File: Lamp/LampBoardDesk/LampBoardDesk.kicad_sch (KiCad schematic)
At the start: 87 parts, among them IC1 L7805ABD2T-TR, IC2 SN74LVC2T45DCUR, J1 DS1023-1x3SF11, J2 DS1023-1x3SF11, J3 284514-3, J4 DC-005-A250, Q1 CMN3406M, SW1 PEC11R, SW2 MT-0-102, U1 RP2040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

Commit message: boards are done
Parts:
- removed H4: MountingHole_Pad, MountingHole:MountingHole_2.7mm_M2.5_DIN965_Pad, symbol Mechanical:MountingHole_Pad
- removed J3: 284514-3, 284514-3:SHDR3W80P0X350_1X3_1250X725X940P, symbol 284514-3:284514-3
- added J3: 284514-3, easyeda2kicad:CONN-TH_3P-P3.50_15EDGRC-3.5-03P, symbol easyeda2kicad:15EDGRC-3.5-03P-14-00A(H)
- J1, J2: footprint easyeda2kicad:HDR-TH_3P-P2.54-V-F-1 -> easyeda2kicad:CONN-SMD-3P-P1.00_BM03B-SRSS-TB-LF-SN; symbol easyeda2kicad:DS1023-1X3SF11 -> easyeda2kicad:BM03B-SRSS-TB(LF)(SN); LCSC C7509516 -> C160389; LCSC Part C7509516 -> C160389
- SW2: footprint easyeda2kicad:SW-TH_MT-0-102-E001-T000-RS-PJ -> easyeda2kicad:SW-TH_MT-0-102-C004-N004-RS; symbol easyeda2kicad:MT-0-102-E001-T000-RS -> easyeda2kicad:MT-0-102-C004-N004-RS; LCSC C1788499 -> C1788496; LCSC Part C1788499 -> C1788496
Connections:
- net +24V: now also SW2.1, J3.3; no longer SW2.3
- net BOOT_LED: now also U1.30 (GPIO19); no longer U1.36 (GPIO24)
- net BTN: now also U1.38 (GPIO26_ADC0); no longer U1.8 (GPIO6)
- net BTN_LED: now also U1.39 (GPIO27_ADC1); no longer U1.7 (GPIO5)
- net ENC_A: now also U1.36 (GPIO24); no longer U1.14 (GPIO11)
- net ENC_B: now also U1.37 (GPIO25); no longer U1.13 (GPIO10)
- net GND: now also J1.4, J1.5, J2.4, J2.5, SW2.4, SW2.5
- net LED_D_O: now also J3.2
- net LED_EN: now also U1.29 (GPIO18); no longer U1.15 (GPIO12)
- net LED_EN_LED: now also U1.14 (GPIO11); no longer U1.4 (GPIO2)
- net MGR_LED: now also U1.4 (GPIO2); no longer U1.5 (GPIO3)
- net P_SEN: now also SW2.3; no longer SW2.1
- net P_SEN_LED: now also U1.8 (GPIO6); no longer U1.37 (GPIO25)
- net P_SEN_O: now also U1.2 (GPIO0); no longer U1.38 (GPIO26_ADC0)
- net SW_CLK: now also J1.1; no longer J1.3
- net SW_D: now also J1.3; no longer J1.1
- net UART_RX: now also J2.3, U1.12 (GPIO9); no longer J2.1, U1.3 (GPIO1)
- net UART_TX: now also J2.1, U1.11 (GPIO8); no longer J2.3, U1.2 (GPIO0)
- net at Q1.3 (D): now also J3.1
- no-connect marks 19 -> 18
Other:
- note added: "Prog"
- note removed: "Program"
- moved on the sheet: C4, C5, C6, D11, D12, IC1, J4

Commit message: Final version ready to roll
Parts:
- removed D12: D_Schottky, Diode_SMD:D_SMA, symbol Device:D_Schottky
- removed D13: GREEN, LED_SMD:LED_0603_1608Metric, symbol Device:LED
- removed J2: DS1023-1x3SF11, easyeda2kicad:CONN-SMD-3P-P1.00_BM03B-SRSS-TB-LF-SN, symbol easyeda2kicad:BM03B-SRSS-TB(LF)(SN)
- removed R24, R25: 2.4k, Resistor_SMD:R_0805_2012Metric, symbol Device:R_Small_US
- removed R26, R27: 330, Resistor_SMD:R_0603_1608Metric, symbol Device:R_Small_US
- removed U3, U4: LTV357T-B, easyeda2kicad:SOP-4_L4.4-W4.0-P2.54-LS7.0-TL, symbol easyeda2kicad:LTV357T-B
- added H4: MountingHole_Pad, MountingHole:MountingHole_2.7mm_M2.5_DIN965_Pad, symbol Mechanical:MountingHole_Pad
- added Q2: FH38P03G6, easyeda2kicad:DFN-8_L3.3-W3.3-P0.65-BL-EP, symbol easyeda2kicad:FH38P03G6
- C8: LCSC C15195 -> C92487; LCSC Part C15195 -> C92487
- CR1: footprint LD1117S33CTR:SOT-223_STM -> easyeda2kicad:SOT-223-4_L6.5-W3.5-P2.30-LS7.0-BR; symbol LD1117S33CTR:LD1117S33CTR -> easyeda2kicad:LD1117S33CTR
- J3: LCSC C7466034 -> C5160226
- R17: value 330 -> 10k; LCSC C23138 -> C15401; LCSC Part C23138 -> C15401
- R19: value 100 -> 10k; LCSC C22775 -> C15401; LCSC Part C22775 -> C15401
- R20: value 1K -> 10k; footprint Resistor_SMD:R_0402_1005Metric -> Resistor_SMD:R_0603_1608Metric; LCSC C25543 -> C15401; LCSC Part C25543 -> C15401
- R21, R22, R23, R8: value 10K -> 10k
- SW1: LCSC (none) -> C143797; LCSC Part (none) -> C143797
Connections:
- net P_SEN is gone; now on net +24V: SW2.3
- net +24V: now also R17.2, Q2.1 (S), Q2.2 (S), Q2.3 (S); no longer C4.1, J3.3, SW2.1
- net +3.3V: now also C8.2, CR1.4 (VOUT); no longer C8.1
- net +5V: now also C7.2; no longer C7.1
- net GND: now also C7.1, C8.1, J3.1, R10.2, R20.1, R9.2, H4.1; no longer C7.2, C8.2, R10.1, R17.2, R20.2, R9.1
- net LED_D: now also IC2.6 (B2), U1.15 (GPIO12); no longer IC2.7 (B1), U1.28 (GPIO17)
- net LED_EN: now also Q1.1 (G), R20.2, U1.14 (GPIO11); no longer U1.29 (GPIO18)
- net LED_EN_LED: now also U1.3 (GPIO1); no longer U1.14 (GPIO11)
- net SW_CLK: now also J1.3; no longer J1.1
- net SW_D: now also J1.1; no longer J1.3
- net at R19.2: now also R17.1, Q2.4 (G)
- net at Q1.3 (D): now also R19.1; no longer J3.1
- net at IC2.3 (A2): now also R11.2; no longer R10.2
- net at IC2.2 (A1): now also R10.1; no longer R11.2
- net P_SEN_LED: no longer names the net of U1.8 (GPIO6)
- net P_SEN_O: no longer names the net of U1.2 (GPIO0)
- net UART_RX: no longer names the net of U1.12 (GPIO9)
- net UART_TX: no longer names the net of U1.11 (GPIO8)
- new net: C4.1, J3.3, Q2.5 (D), Q2.6 (D), Q2.7 (D), Q2.8 (D)
- new net: IC2.7 (B1), R9.1
- no-connect marks 18 -> 24
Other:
- note removed: "Party"
- moved on the sheet: C4, C7, C8, D1, D2, D3, D4, D9, J1, J3, R10, R11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

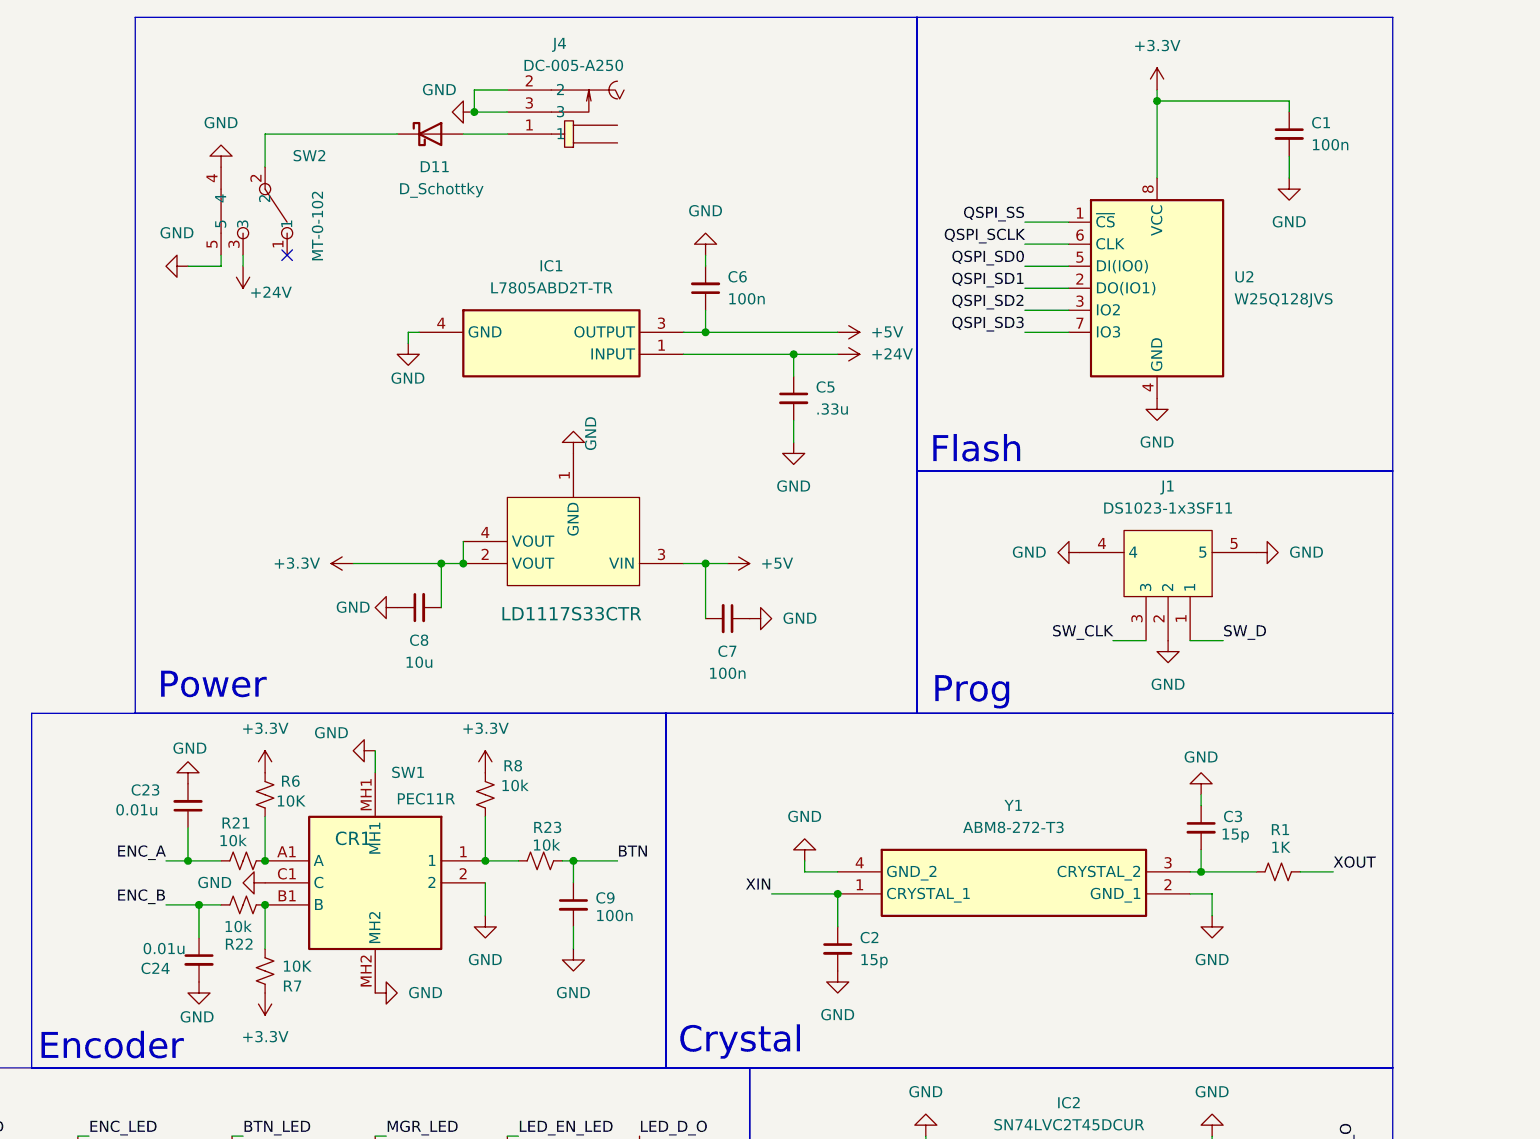
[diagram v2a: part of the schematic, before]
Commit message: Finished lamp saving; cad v0.4
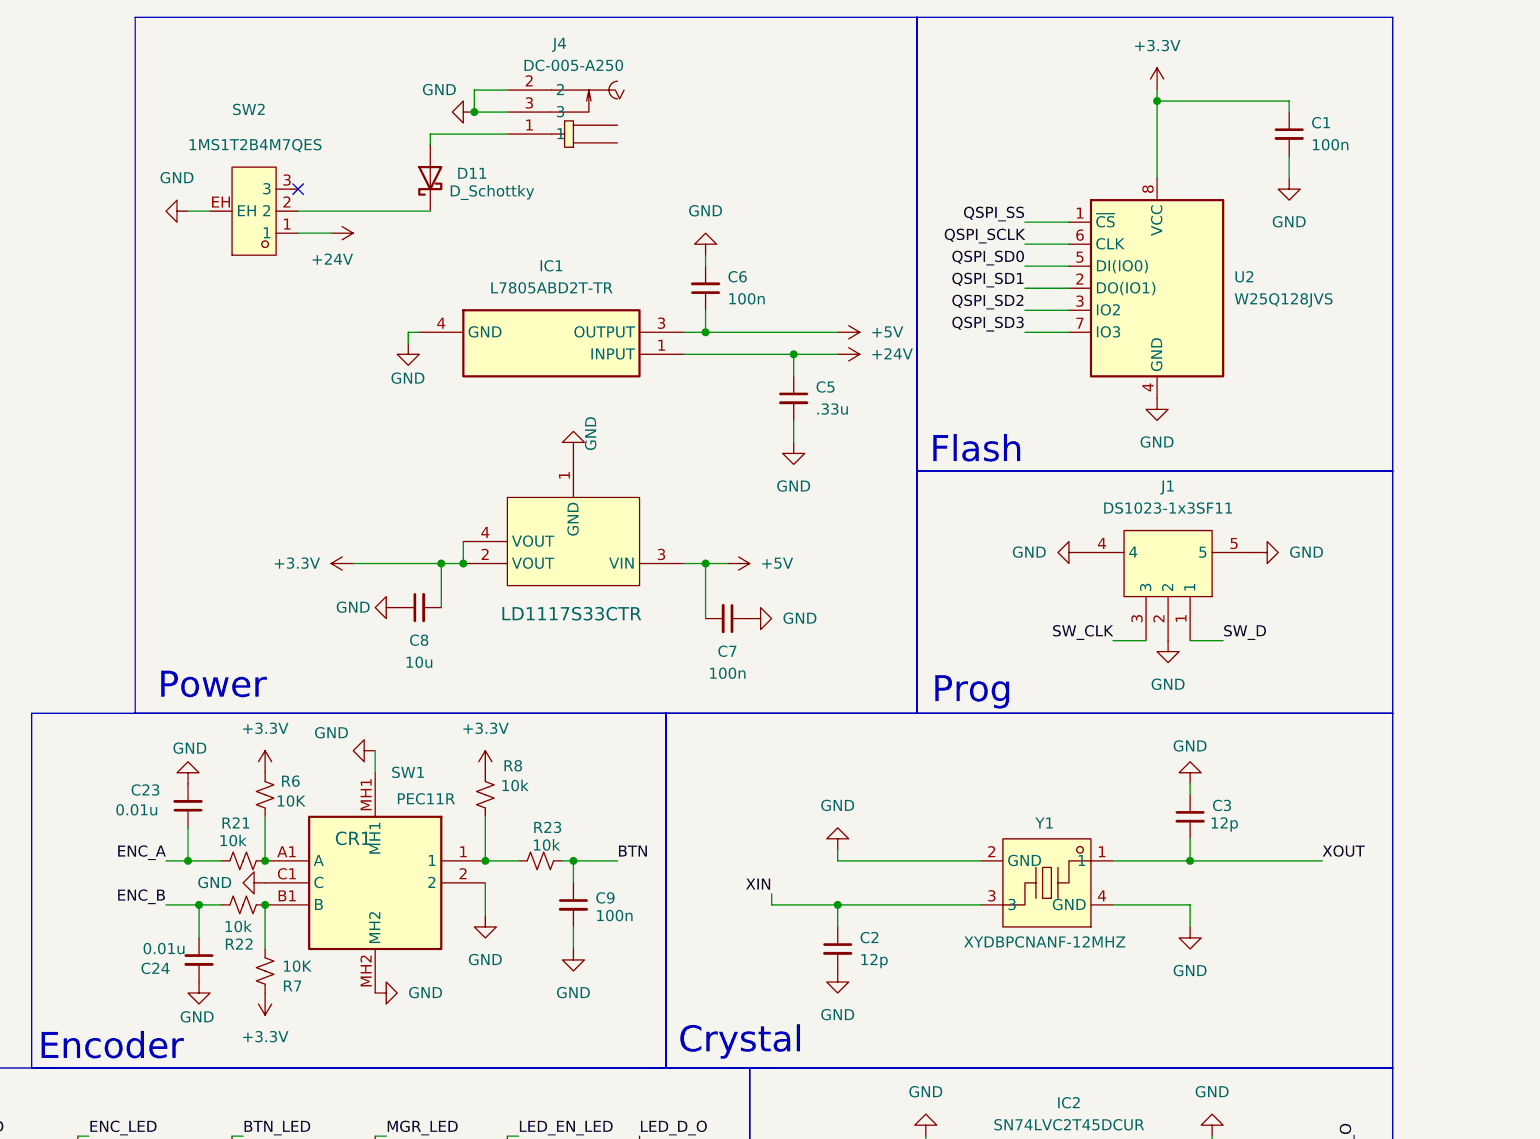
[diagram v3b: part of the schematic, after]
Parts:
- removed R1: 1K, Resistor_SMD:R_0402_1005Metric, symbol Device:R_Small_US
- C2, C3: value 15p -> 12p; LCSC C86285 -> C1547; LCSC Part C86285 -> C1547
- SW2: value MT-0-102 -> 1MS1T2B4M7QES; footprint easyeda2kicad:SW-TH_MT-0-102-C004-N004-RS -> easyeda2kicad:SW-TH_1MS1T2B4M7QES; symbol easyeda2kicad:MT-0-102-C004-N004-RS -> easyeda2kicad:1MS1T2B4M7QES; LCSC C1788496 -> C496157; LCSC Part C1788496 -> C496157
- Y1: value ABM8-272-T3 -> XYDBPCNANF-12MHZ; footprint ABM8-272-T3:ABM8272T3 -> easyeda2kicad:OSC-SMD_4P-L2.5-W2.0-BL; symbol ABM8-272-T3:ABM8-272-T3 -> easyeda2kicad:XYDBPCNANF-12MHZ; LCSC C20625731 -> C521567; LCSC Part C20625731 -> C521567
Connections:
- net +24V: now also SW2.1; no longer SW2.3
- net GND: now also SW2.EH; no longer SW2.4, SW2.5
- net XIN: now also Y1.3; no longer Y1.1 (CRYSTAL_1)
- net XOUT: now also C3.2, Y1.1
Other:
- moved on the sheet: C3, D11
